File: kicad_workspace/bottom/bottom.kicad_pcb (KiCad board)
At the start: 2 copper layers, 76.8 x 84 mm, 53 parts, among them J1 Battery connector, J2 Battery connector, M1 N20_MOTOR_EXTENDED_SHAFT, M2 N20_MOTOR_EXTENDED_SHAFT, U1 DRV8833PWP, U3 STM32F303RETx, U4 BNO055, Y1 32.768kHz, Y2 8MHz, Y3 32.768kHz

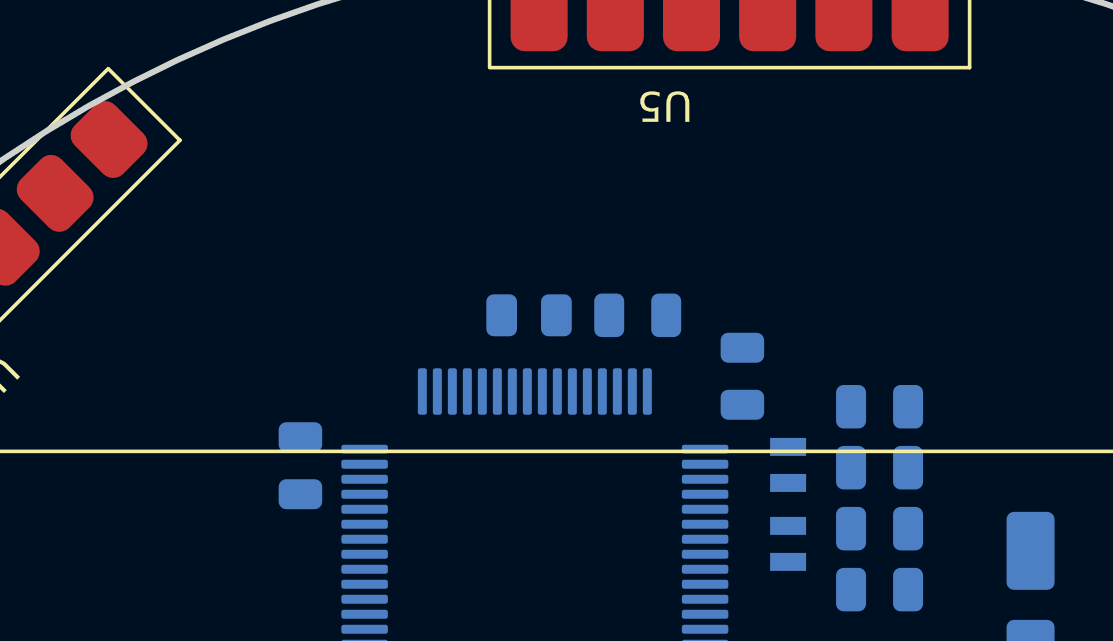
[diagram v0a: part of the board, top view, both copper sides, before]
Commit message: add tp5100 li ion charger module
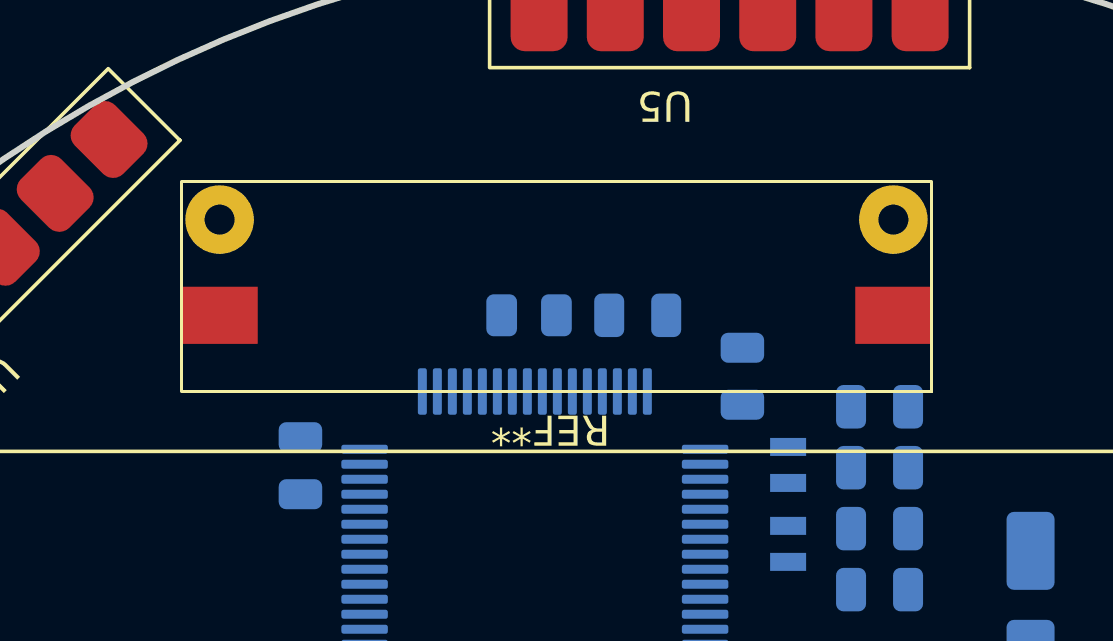
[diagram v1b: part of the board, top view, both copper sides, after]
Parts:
- added REF**: TP5100, pololu:TP5100, F.Cu at (67.3, 33.0)
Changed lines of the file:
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@@
+    )
+  )
+  (footprint "pololu:TP5100" (layer "F.Cu")
+    (at 67.31 33.02 180)
+    (attr through_hole)
+    (fp_text reference "REF**" (at 12.7 -1.27 180 unlocked) (layer "F.SilkS")
+        (effects (font (size 1 1) (thickness 0.1)))
+    )
+    (fp_text value "TP5100" (at 12.7 1 180 unlocked) (layer "F.Fab")
+        (effects (font (size 1 1) (thickness 0.15)))
+    )
+    (fp_text user "${REFERENCE}" (at 12.7 2.54 180 unlocked) (layer "F.Fab")
+        (effects (font (size 1 1) (thickness 0.15)))
+    )
+    (fp_rect (start 0 0) (end 25 7)
+      (stroke (width 0.1) (type default)) (fill none) (layer "F.SilkS"))
+    (pad "1" smd rect (at 1.27 2.54 180) (size 2.54 1.905) (layers "F.Cu" "F.Paste" "F.Mask")
+      (thermal_bridge_angle 45))
+    (pad "2" smd rect (at 23.73 2.54 180) (size 2.54 1.905) (layers "F.Cu" "F.Paste" "F.Mask")
+      (thermal_bridge_angle 45))
+    (pad "3" thru_hole circle (at 1.27 5.73 180) (size 2.286 2.286) (drill 1) (layers "*.Cu" "*.Mask"))
+    (pad "4" thru_hole circle (at 23.73 5.73 180) (size 2.286 2.286) (drill 1) (layers "*.Cu" "*.Mask"))
+    (model "${KIPRJMOD}/../3d_models/tp5100.step"
+      (offset (xyz 12.5 -1.6 8))
+      (scale (xyz 1 1 1))
+      (rotate (xyz 0 90 -90))
     )
   )

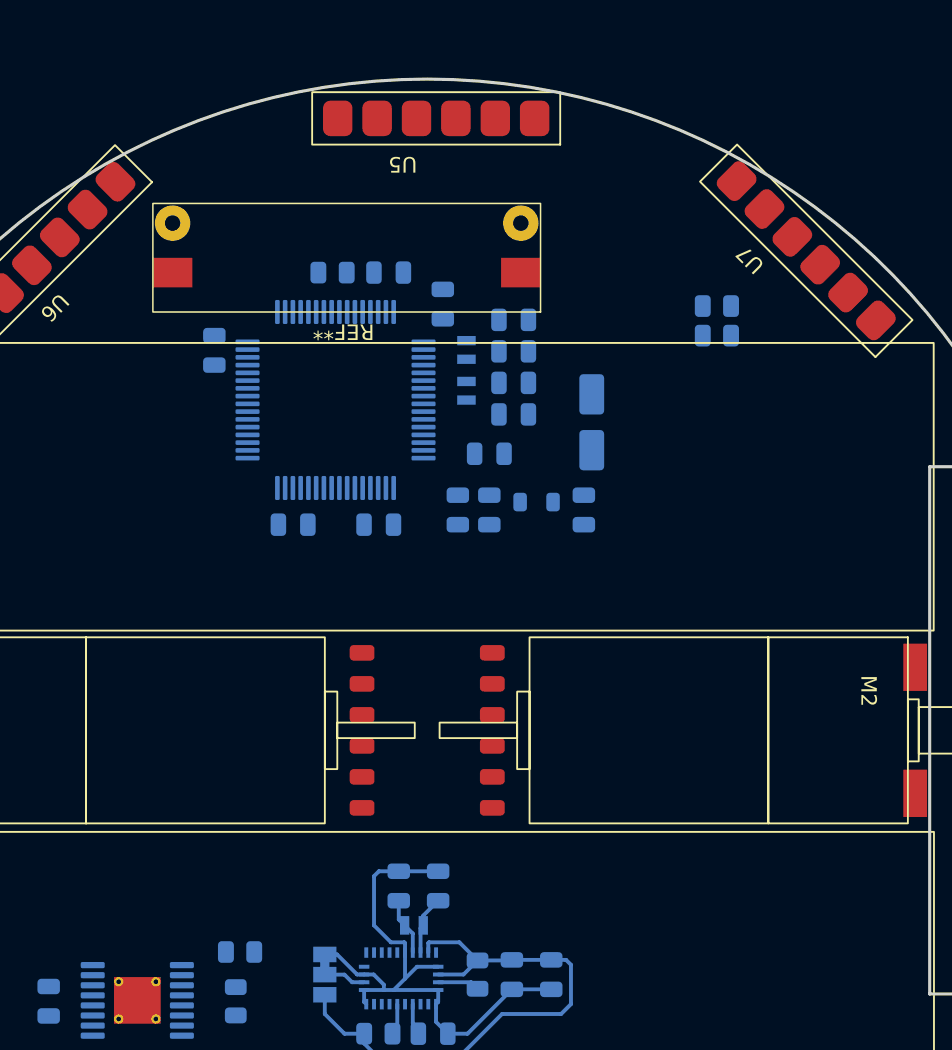
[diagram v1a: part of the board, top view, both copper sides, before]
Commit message: add copper pads for charging
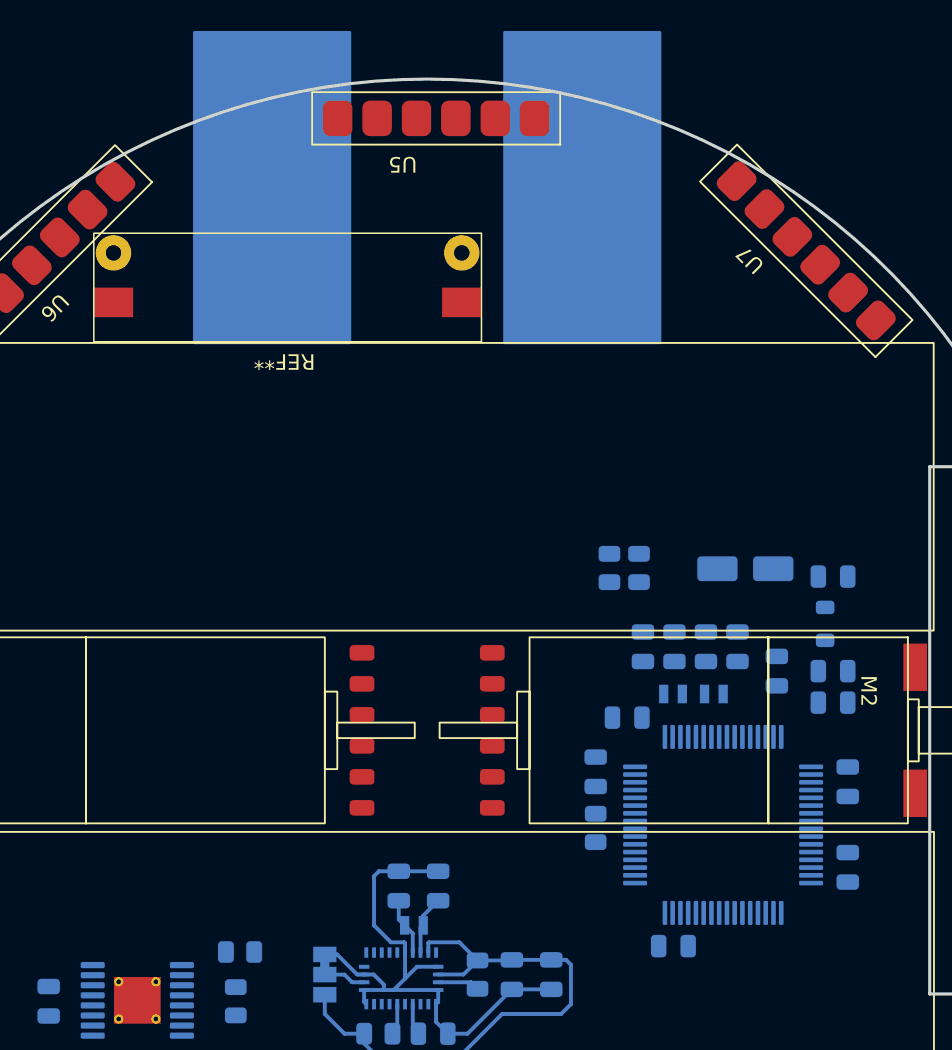
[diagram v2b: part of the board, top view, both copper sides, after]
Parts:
- moved C12 48.5 mm to (75.9, 73.9), turned to 0 degrees
- moved C13 42.0 mm to (87.1, 68.8), turned to 90 degrees
- moved R3 39.6 mm to (70.9, 66.3), turned to -90 degrees
- moved U3 37.1 mm to (79.1, 66.1), turned to -90 degrees
- moved C15 34.9 mm to (70.9, 62.7), turned to -90 degrees
- moved C14 34.5 mm to (87.1, 63.3), turned to 90 degrees
- moved C11 29.2 mm to (72.9, 59.2), turned to 180 degrees
- moved C17 27.2 mm to (86.2, 58.2), turned to 0 degrees
- moved Y3 25.9 mm to (75.9, 57.7), turned to 180 degrees
- moved Y2 25.2 mm to (78.5, 57.7), turned to 180 degrees
- moved C16 24.5 mm to (86.2, 56.2), turned to 0 degrees
- moved C10 23.2 mm to (82.5, 56.2), turned to 90 degrees
- moved C21 22.7 mm to (73.9, 54.6), turned to -90 degrees
- moved C20 21.7 mm to (75.9, 54.6), turned to -90 degrees
- moved C19 21.1 mm to (78.0, 54.6), turned to -90 degrees
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
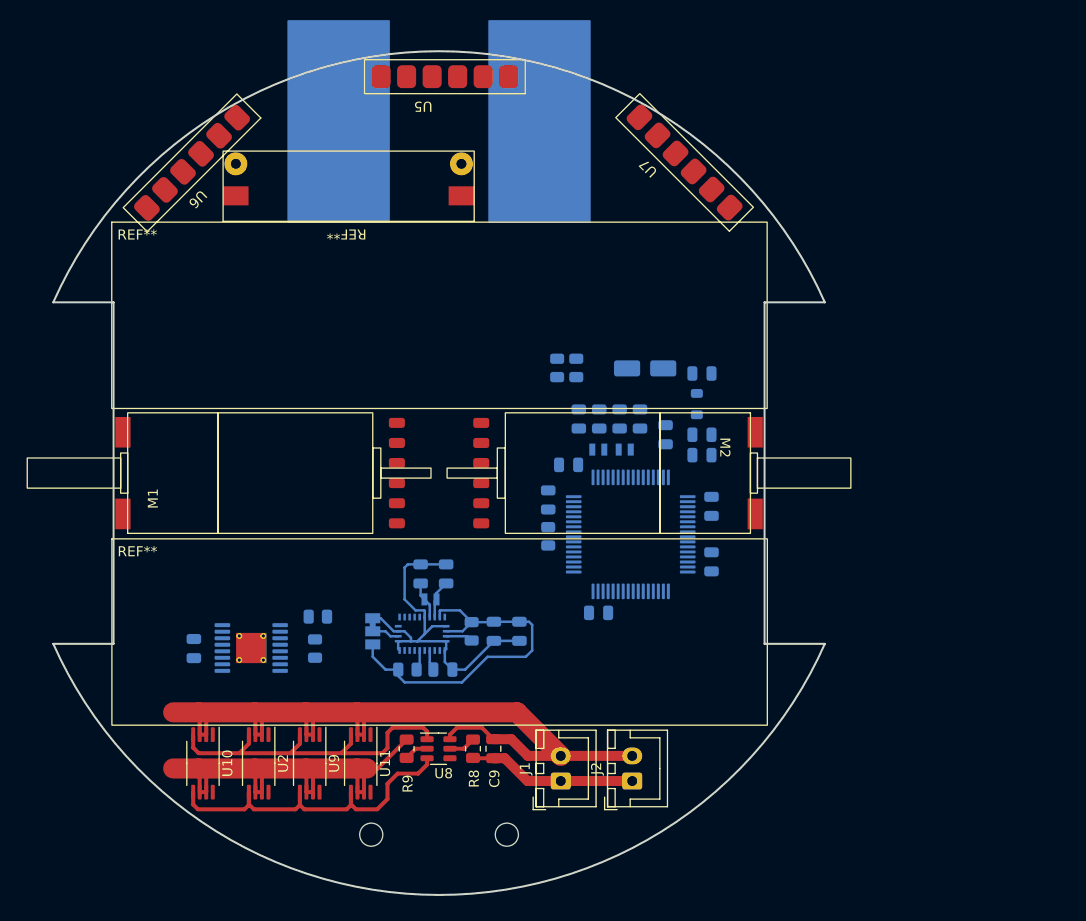
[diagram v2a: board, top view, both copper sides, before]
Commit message: add all modules to pcb (except termometer)
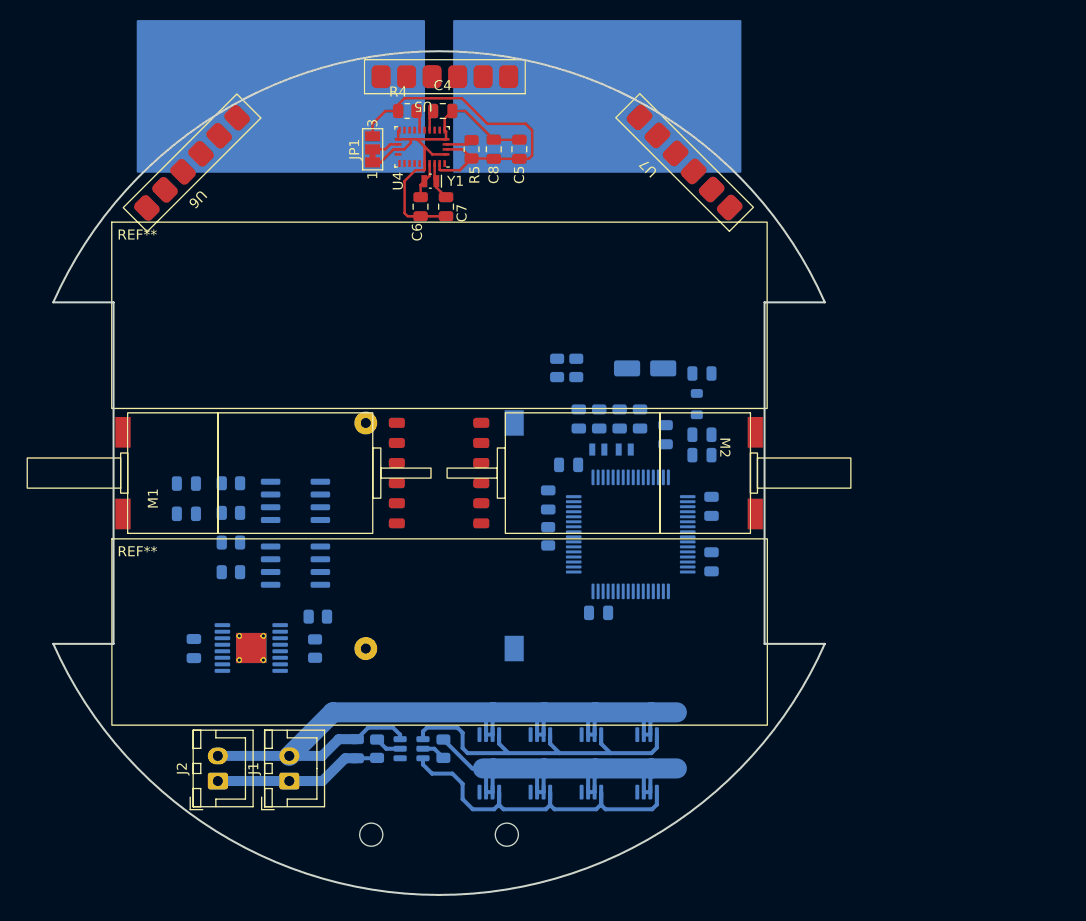
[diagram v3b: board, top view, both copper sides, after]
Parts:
- added C22: 100nF, Capacitor_SMD:C_0805_2012Metric, B.Cu at (34.8, 61.0)
- added C23: 100nF, Capacitor_SMD:C_0805_2012Metric, B.Cu at (34.8, 64.1)
- added R10: 10K, Resistor_SMD:R_0805_2012Metric, B.Cu at (39.3, 61.0)
- added R11: 10K, Resistor_SMD:R_0805_2012Metric, B.Cu at (39.3, 64.0)
- added R12: 10K, Resistor_SMD:R_0805_2012Metric, B.Cu at (39.3, 66.9)
- added R13: 10K, Resistor_SMD:R_0805_2012Metric, B.Cu at (39.3, 69.9)
- added REF**: U3V70F5, pololu:U3V70F5, B.Cu at (69.8, 47.0)
- added REF**: S7V8F3, pololu:S7V8F3, B.Cu at (90.1, 43.1)
- added U12: ACS712-5A, Package_SO:SOIC-8_3.9x4.9mm_P1.27mm, B.Cu at (45.7, 62.8)
- added U13: ACS712-5A, Package_SO:SOIC-8_3.9x4.9mm_P1.27mm, B.Cu at (45.7, 69.2)
- C4, C5, C6, C7, C8, JP1, R4, R5, U4, Y1: moved to F.Cu
- C9, R8, R9, REF**, U10, U11, U2, U8, U9: moved to B.Cu
- moved C4 55.6 mm to (60.4, 24.0)
- moved R4 55.6 mm to (56.8, 24.0)
- moved U4 48.5 mm to (58.3, 27.5)
- moved C5 48.0 mm to (68.0, 27.8), turned to 90 degrees
- moved C8 48.0 mm to (65.5, 27.8), turned to 90 degrees
- moved JP1 48.0 mm to (53.4, 27.8), turned to 90 degrees
- moved R5 48.0 mm to (63.2, 27.8), turned to -90 degrees
- moved U10 44.2 mm to (80.7, 88.9)
- moved Y1 41.6 mm to (59.1, 30.9)
- moved J2 41.3 mm to (38.0, 90.7)
- moved C6 36.6 mm to (58.2, 33.5), turned to -90 degrees
- moved C7 36.6 mm to (60.7, 33.5), turned to -90 degrees
- moved U2 33.1 mm to (75.2, 88.9)
- moved J1 27.0 mm to (45.1, 90.7)
- moved U9 23.0 mm to (70.1, 88.9)
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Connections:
- U1 pad 4: Net-(M1-M2) -> Net-(U1-AOUT2)
- U1 pad 5: Net-(M2-M2) -> Net-(U1-BOUT2)

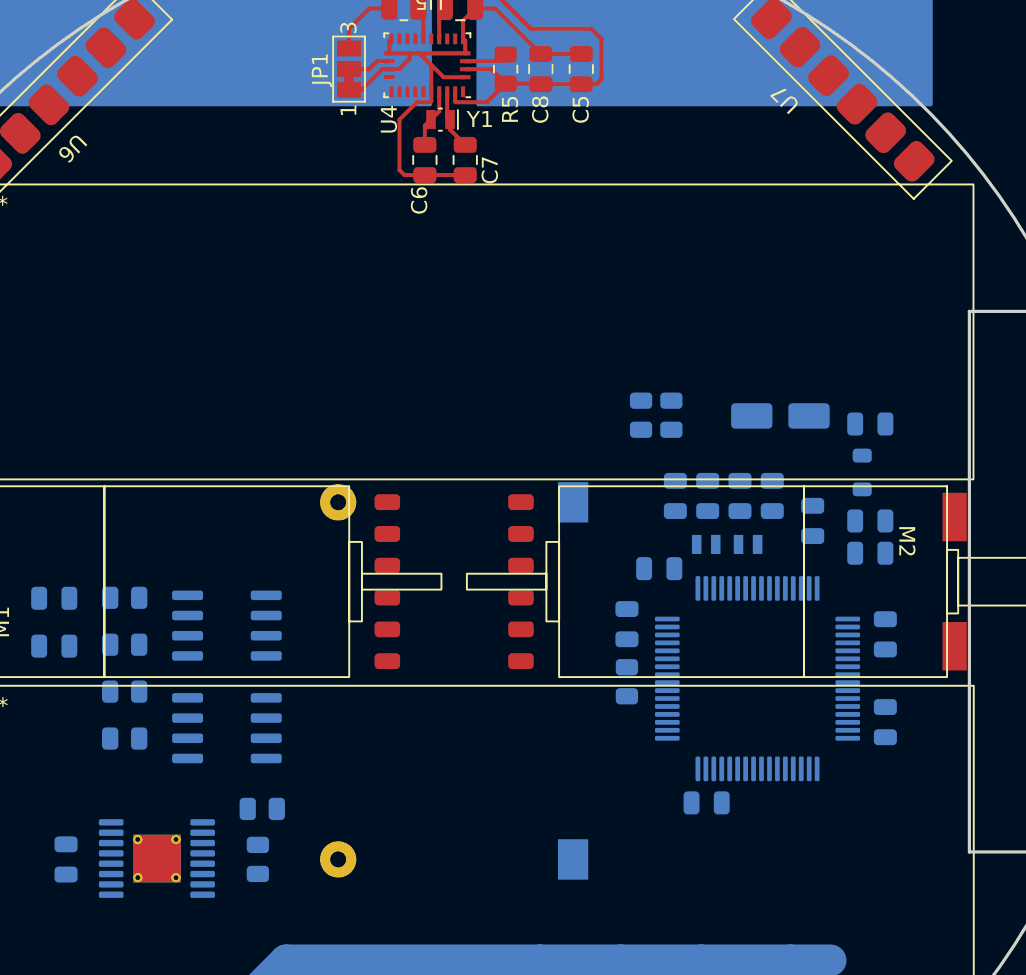
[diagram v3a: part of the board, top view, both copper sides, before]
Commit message: add batt_prot symbol. clean schematic
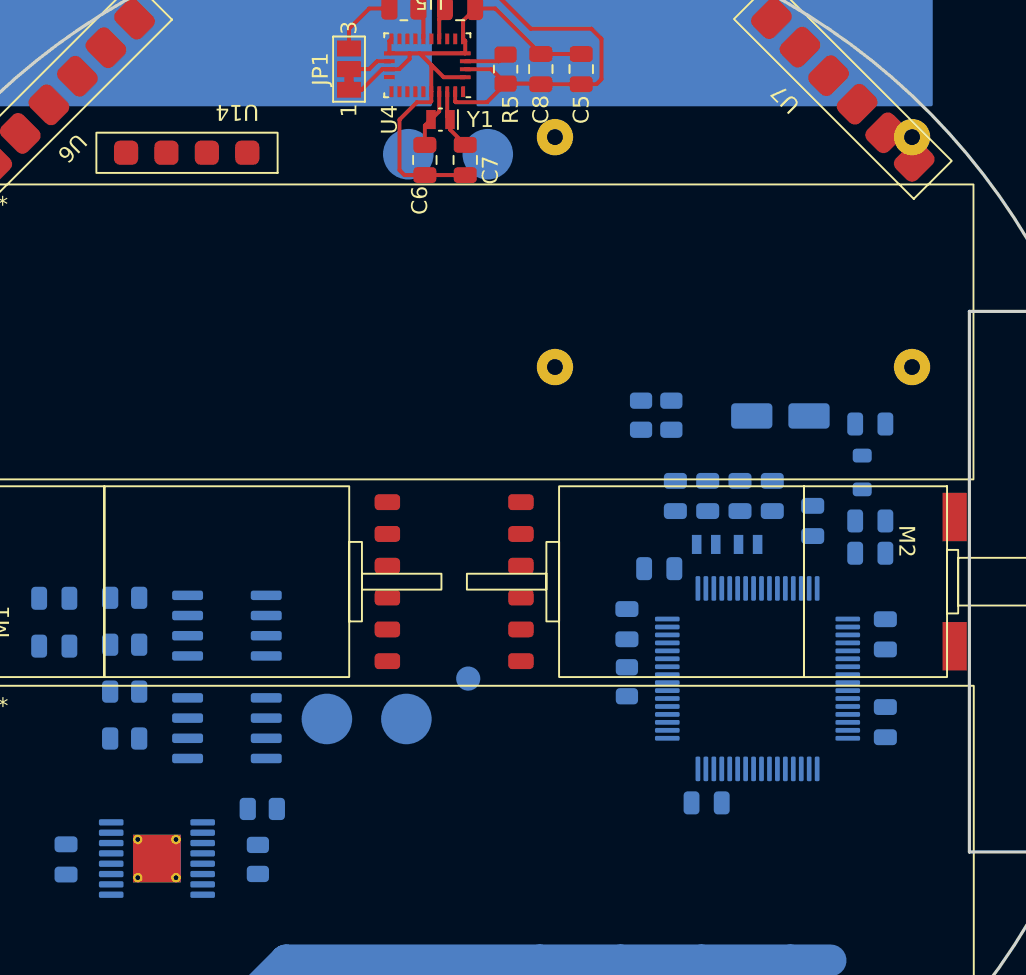
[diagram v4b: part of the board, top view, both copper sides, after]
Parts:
- removed the REF** at (69.8, 47.0)
- removed the REF** at (51.4, 53.7)
- removed the REF** at (90.1, 43.1)
- added U14: ~, pololu:S7V8F3_vertical, F.Cu at (48.9, 34.3)
- added U15: ~, pololu:U3V70F5, B.Cu at (64.7, 30.6)
- added U16: ~, pololu:TP5100, B.Cu at (65.1, 47.8)
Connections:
- net Net-(M1-M2) renamed IP_MOTOR_A+
- net Net-(M2-M2) renamed IP_MOTOR_B+
- net Net-(U1-AOUT2) renamed IP_MOTOR_A-
- net Net-(U1-BOUT2) renamed IP_MOTOR_B-
- C10 pad 2: GND -> -BATT_PROT
- C11 pad 2: GND -> -BATT_PROT
- C12 pad 2: GND -> -BATT_PROT
- C13 pad 2: GND -> -BATT_PROT
- C14 pad 2: GND -> -BATT_PROT
- C15 pad 2: GND -> -BATT_PROT
- C16 pad 2: GND -> -BATT_PROT
- C17 pad 2: GND -> -BATT_PROT
- C18 pad 1: GND -> -BATT_PROT
- C19 pad 1: GND -> -BATT_PROT
- C2 pad 2: GND -> -BATT_PROT
- C20 pad 1: GND -> -BATT_PROT
- C21 pad 1: GND -> -BATT_PROT
- C22 pad 2: GND -> -BATT_PROT
- C23 pad 2: GND -> -BATT_PROT
- C3 pad 2: GND -> -BATT_PROT
- C4 pad 2: GND -> -BATT_PROT
- C5 pad 2: GND -> -BATT_PROT
- C6 pad 2: GND -> -BATT_PROT
- C7 pad 2: GND -> -BATT_PROT
- C8 pad 2: GND -> -BATT_PROT
- JP1 pad 1: GND -> -BATT_PROT
- M1 pad 1: GND -> -BATT_PROT
- M2 pad 1: GND -> -BATT_PROT
- R1 pad 1: GND -> -BATT_PROT
- R11 pad 1: GND -> -BATT_PROT
- R13 pad 1: GND -> -BATT_PROT
- R2 pad 1: GND -> -BATT_PROT
- R3 pad 2: GND -> -BATT_PROT
- R9 pad 1: Net-(R9-Pad1) -> -BATT_PROT
- U1 pad 13: GND -> -BATT_PROT
- U1 pad 17: GND -> -BATT_PROT
- U10 pad 6: Net-(R9-Pad1) -> -BATT_PROT
- U10 pad 7: Net-(R9-Pad1) -> -BATT_PROT
- U11 pad 6: Net-(R9-Pad1) -> -BATT_PROT
- U11 pad 7: Net-(R9-Pad1) -> -BATT_PROT
- U12 pad 5: GND -> -BATT_PROT
- U13 pad 5: GND -> -BATT_PROT
- U2 pad 6: Net-(R9-Pad1) -> -BATT_PROT
- U2 pad 7: Net-(R9-Pad1) -> -BATT_PROT
- U3 pad 12: GND -> -BATT_PROT
- U3 pad 18: GND -> -BATT_PROT
- U3 pad 31: GND -> -BATT_PROT
- U3 pad 47: GND -> -BATT_PROT
- U3 pad 63: GND -> -BATT_PROT
- U4 pad 15: GND -> -BATT_PROT
- U4 pad 16: GND -> -BATT_PROT
- U4 pad 18: GND -> -BATT_PROT
- U4 pad 2: GND -> -BATT_PROT
- U4 pad 25: GND -> -BATT_PROT
- U4 pad 5: GND -> -BATT_PROT
- U4 pad 6: GND -> -BATT_PROT
- U5 pad 2: GND -> -BATT_PROT
- U6 pad 2: GND -> -BATT_PROT
- U7 pad 2: GND -> -BATT_PROT
- U9 pad 6: Net-(R9-Pad1) -> -BATT_PROT
- U9 pad 7: Net-(R9-Pad1) -> -BATT_PROT
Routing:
- net -BATT_PROT: track 0.00 -> 85.1 mm
- net Net-(R9-Pad1): track 47.2 -> 0.00 mm
- net GND: track 37.9 -> 0.00 mm
